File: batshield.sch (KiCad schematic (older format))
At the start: 57 parts, among them J1 mic in, J2 Audio-Jack-2, J3 Audio-Jack-2, J6 Audio-Jack-2, J7 DIN-5_180degree, J8 DIN-5_180degree, SW1 SW_SPDT, SW2 SW_SPDT, SW3 SW_SPDT, SW4 SW_SPST, SW5 SW_Push, SW6 SW_SPST, SW7 SW_Push, SW8 SW_SPST, SW9 SW_Push, U1 LM741, U2 4N35

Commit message: todos los elementos añadidos
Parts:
- removed J?: left up pins, symbol Conn_01x03_Male
- added J?: left up pins, symbol Conn_01x04_Male
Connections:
- net labels added: D7, D8, VIN
- wire segments 154 -> 151
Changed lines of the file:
@@
 	2200 4600 2500 4600
 Wire Wire Line
-	1300 4500 1350 4500
-Wire Wire Line
-	1350 4500 1450 4500
+	1300 4500 1450 4500
 Connection ~ 2900 4100
 Wire Wire Line
@@
 	2900 4850 2900 4800
 Wire Wire Line
-	2750 4800 2900 4800
-Wire Wire Line
-	2900 4800 3000 4800
+	2750 4800 3000 4800
 Wire Wire Line
 	2300 4800 2450 4800
@@
 Connection ~ 4200 4700
 Wire Wire Line
-	4000 4700 4050 4700
-Wire Wire Line
-	4050 4700 4200 4700
-Wire Wire Line
-	4200 4700 4550 4700
+	4000 4700 4550 4700
 Wire Wire Line
 	4200 4350 4200 4150
@@
 	4200 5050 4200 5300
 Wire Wire Line
-	4200 4650 4200 4700
-Wire Wire Line
-	4200 4700 4200 4750
+	4200 4650 4200 4750
 Wire Wire Line
 	3600 4700 3700 4700
@@
 Connection ~ 2900 4600
 Wire Wire Line
-	2900 3950 2900 4100
-Wire Wire Line
-	2900 4100 2900 4600
+	2900 3950 2900 4600
 Wire Wire Line
 	3100 4100 2900 4100
 Wire Wire Line
-	2800 4600 2900 4600
-Wire Wire Line
-	2900 4600 3000 4600
+	2800 4600 3000 4600
 Wire Wire Line
 	1900 1900 4150 1900
@@
 	1900 2100 2100 2100
 Wire Wire Line
-	2400 2100 2550 2100
-Wire Wire Line
-	2550 2100 2950 2100
-Wire Wire Line
-	2950 2100 3100 2100
+	2400 2100 3100 2100
 Connection ~ 3550 3050
 Wire Wire Line
@@
 Connection ~ 4150 2100
 Wire Wire Line
-	3550 3000 3550 3050
-Wire Wire Line
-	3550 3050 3550 3200
-Wire Wire Line
-	2550 3050 3550 3050
-Wire Wire Line
-	3550 3050 4350 3050
+	3550 3000 3550 3200
+Wire Wire Line
+	2550 3050 4350 3050
 Wire Wire Line
 	2550 2500 2550 3050
 Wire Wire Line
-	4000 2100 4150 2100
-Wire Wire Line
-	4150 2100 4450 2100
+	4000 2100 4450 2100
 Wire Wire Line
 	4150 2600 4100 2600
@@
 Connection ~ 3550 2600
 Wire Wire Line
-	3550 2500 3550 2600
-Wire Wire Line
-	3550 2600 3550 2700
-Wire Wire Line
-	3300 2600 3550 2600
-Wire Wire Line
-	3550 2600 3800 2600
+	3550 2500 3550 2700
+Wire Wire Line
+	3300 2600 3800 2600
 Connection ~ 3550 2100
 Wire Wire Line
 	3550 2200 3550 2100
 Wire Wire Line
-	3400 2100 3550 2100
-Wire Wire Line
-	3550 2100 3700 2100
+	3400 2100 3700 2100
 Connection ~ 2550 2100
 Wire Wire Line
@@
 	6050 1250 6300 1250
 Wire Wire Line
-	6600 1250 6750 1250
-Wire Wire Line
-	6750 1250 6950 1250
+	6600 1250 6950 1250
 Wire Wire Line
 	6950 1950 6950 1450
 Wire Wire Line
-	6050 1950 6750 1950
-Wire Wire Line
-	6750 1950 6950 1950
+	6050 1950 6950 1950
 Wire Wire Line
 	6750 1450 6750 1250
@@
 	7750 850  7750 750
 Wire Wire Line
-	7550 1350 7750 1350
-Wire Wire Line
-	7750 1350 7950 1350
+	7550 1350 7950 1350
 Wire Wire Line
 	7750 1150 7750 1350
@@
 	9450 2950 9550 2950
 Wire Wire Line
-	2150 700  2150 900
-Wire Wire Line
-	2150 900  2150 1000
+	2150 700  2150 1000
 Wire Wire Line
 	2150 1350 2150 1300
 Connection ~ 4150 1900
 Wire Wire Line
-	1000 700  1450 700
-Wire Wire Line
-	1450 700  1600 700
+	1000 700  1600 700
 Connection ~ 1450 700
 Wire Wire Line
@@
 	1450 2000 1500 2000
 Wire Wire Line
-	1450 700  1450 900
-Wire Wire Line
-	1450 900  1450 1800
+	1450 700  1450 1800
 Wire Wire Line
 	1450 900  1600 900
 Connection ~ 1450 900
 Wire Wire Line
-	1900 900  2150 900
-Wire Wire Line
-	2150 900  4150 900
+	1900 900  4150 900
 Connection ~ 2150 900
 Wire Wire Line
 	1900 700  2150 700
 Wire Wire Line
-	4150 900  4150 1900
-Wire Wire Line
-	4150 1900 4150 2100
-Wire Wire Line
-	4150 2100 4150 2600
+	4150 900  4150 2600
 Wire Wire Line
 	6200 4500 6100 4500
@@
 	6100 4500 6100 4650
 Wire Wire Line
-	6600 4500 6750 4500
-Wire Wire Line
-	6750 4500 7000 4500
+	6600 4500 7000 4500
 Wire Wire Line
 	6750 4400 6750 4500
@@
 	7400 4500 7400 4650
 Wire Wire Line
-	7900 4500 8050 4500
-Wire Wire Line
-	8050 4500 8300 4500
+	7900 4500 8300 4500
 Wire Wire Line
 	8050 4400 8050 4500
@@
 	8800 4500 8800 4650
 Wire Wire Line
-	9300 4500 9450 4500
-Wire Wire Line
-	9450 4500 9700 4500
+	9300 4500 9700 4500
 Wire Wire Line
 	9450 4400 9450 4500
@@
 	6100 5550 6100 5700
 Wire Wire Line
-	6600 5550 6750 5550
-Wire Wire Line
-	6750 5550 7000 5550
+	6600 5550 7000 5550
 Wire Wire Line
 	6750 5450 6750 5550
@@
 	7400 5550 7400 5700
 Wire Wire Line
-	7900 5550 8050 5550
-Wire Wire Line
-	8050 5550 8300 5550
+	7900 5550 8300 5550
 Wire Wire Line
 	8050 5450 8050 5550
@@
 	8800 5550 8800 5700
 Wire Wire Line
-	9300 5550 9450 5550
-Wire Wire Line
-	9450 5550 9700 5550
+	9300 5550 9700 5550
 Wire Wire Line
 	9450 5450 9450 5550
@@
 F 3 "" H 3850 7000 50  0001 C CNN
 	1    3850 7000
-	1    0    0    -1
-$EndComp
-$Comp
-L Conn_01x03_Male J?
-U 1 1 59DC708D
-P 3850 6350
-F 0 "J?" H 3850 6550 50  0000 C CNN
-F 1 "left up pins" H 3850 6150 50  0000 C CNN
-F 2 "" H 3850 6350 50  0001 C CNN
-F 3 "" H 3850 6350 50  0001 C CNN
-	1    3850 6350
 	1    0    0    -1
 $EndComp
@@
 	1    0    0    -1
 $EndComp
+Text GLabel 4150 7300 2    60   Input ~ 0
+A5
+Text GLabel 4150 7200 2    60   Input ~ 0
+A4
+Text GLabel 4150 7100 2    60   Input ~ 0
+A3
+Text GLabel 4150 7000 2    60   Input ~ 0
+A2
+Text GLabel 4150 6900 2    60   Input ~ 0
+A1
+Text GLabel 4150 6800 2    60   Input ~ 0
+A0
+$Comp
+L Conn_01x04_Male J?
+U 1 1 59DC8B73
+P 3850 6250
+F 0 "J?" H 3850 6450 50  0000 C CNN
+F 1 "left up pins" H 3850 5950 50  0000 C CNN
+F 2 "" H 3850 6250 50  0001 C CNN
+F 3 "" H 3850 6250 50  0001 C CNN
+	1    3850 6250
+	1    0    0    -1
+$EndComp
+Text GLabel 4150 6450 2    60   Input ~ 0
+VIN
+Text GLabel 4150 6350 2    60   Input ~ 0
+GND
+Text GLabel 4150 6250 2    60   Input ~ 0
+GND
+Text GLabel 4150 6150 2    60   Input ~ 0
++5V
+Text GLabel 3250 6300 2    60   Input ~ 0
+GND
+$Comp
+L GND #PWR?
+U 1 1 59DC9304
+P 3150 6350
+F 0 "#PWR?" H 3150 6100 50  0001 C CNN
+F 1 "GND" H 3150 6200 50  0000 C CNN
+F 2 "" H 3150 6350 50  0001 C CNN
+F 3 "" H 3150 6350 50  0001 C CNN
+	1    3150 6350
+	1    0    0    -1
+$EndComp
+Wire Wire Line
+	3250 6300 3150 6300
+Wire Wire Line
+	3150 6300 3150 6350
+Wire Wire Line
+	4050 6150 4150 6150
+Wire Wire Line
+	4050 6250 4150 6250
+Wire Wire Line
+	4050 6350 4150 6350
+Wire Wire Line
+	4050 6450 4150 6450
+Wire Wire Line
+	4050 6800 4150 6800
+Wire Wire Line
+	4050 6900 4150 6900
+Wire Wire Line
+	4050 7000 4150 7000
+Wire Wire Line
+	4050 7100 4150 7100
+Wire Wire Line
+	4050 7200 4150 7200
+Wire Wire Line
+	4050 7300 4150 7300
+Text GLabel 5200 7300 2    60   Input ~ 0
+RX
+Text GLabel 5200 7200 2    60   Input ~ 0
+TX
+Text GLabel 5200 7100 2    60   Input ~ 0
+D2
+Text GLabel 5200 7000 2    60   Input ~ 0
+D3
+Text GLabel 5200 6900 2    60   Input ~ 0
+D4
+Text GLabel 5200 6800 2    60   Input ~ 0
+D5#
+Text GLabel 5200 6700 2    60   Input ~ 0
+D6#
+Text GLabel 5200 6600 2    60   Input ~ 0
+D7
+Text GLabel 5200 6250 2    60   Input ~ 0
+D8
+Text GLabel 5200 6150 2    60   Input ~ 0
+D9
+Text GLabel 5200 6050 2    60   Input ~ 0
+D10
+Text GLabel 5200 5950 2    60   Input ~ 0
+D11
+Text GLabel 5200 5850 2    60   Input ~ 0
+D12
+Text GLabel 5200 5750 2    60   Input ~ 0
+D13
+Text GLabel 5200 5650 2    60   Input ~ 0
+GND
+Wire Wire Line
+	5100 5650 5200 5650
+Wire Wire Line
+	5100 5750 5200 5750
+Wire Wire Line
+	5100 5850 5200 5850
+Wire Wire Line
+	5100 5950 5200 5950
+Wire Wire Line
+	5100 6050 5200 6050
+Wire Wire Line
+	5100 6150 5200 6150
+Wire Wire Line
+	5100 6250 5200 6250
+Wire Wire Line
+	5100 6600 5200 6600
+Wire Wire Line
+	5100 6700 5200 6700
+Wire Wire Line
+	5100 6800 5200 6800
+Wire Wire Line
+	5100 6900 5200 6900
+Wire Wire Line
+	5100 7000 5200 7000
+Wire Wire Line
+	5100 7100 5200 7100
+Wire Wire Line
+	5100 7200 5200 7200
+Wire Wire Line
+	5100 7300 5200 7300
 $EndSCHEMATC

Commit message: power folags
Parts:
- gave numbers to parts that had none: 4
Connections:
- wire segments 151 -> 153
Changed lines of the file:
@@
 $EndComp
 $Comp
-L GND #PWR7
+L GND #PWR8
 U 1 1 59DB61AD
 P 3550 3200
-F 0 "#PWR7" H 3550 2950 50  0001 C CNN
+F 0 "#PWR8" H 3550 2950 50  0001 C CNN
 F 1 "GND" H 3550 3050 50  0000 C CNN
 F 2 "" H 3550 3200 50  0001 C CNN
@@
 +5V
 $Comp
-L GND #PWR8
+L GND #PWR9
 U 1 1 59DB7354
 P 4200 5300
-F 0 "#PWR8" H 4200 5050 50  0001 C CNN
+F 0 "#PWR9" H 4200 5050 50  0001 C CNN
 F 1 "GND" H 4200 5150 50  0000 C CNN
 F 2 "" H 4200 5300 50  0001 C CNN
@@
 RX
 $Comp
-L GND #PWR15
+L GND #PWR16
 U 1 1 59DBACB5
 P 7750 1800
-F 0 "#PWR15" H 7750 1550 50  0001 C CNN
+F 0 "#PWR16" H 7750 1550 50  0001 C CNN
 F 1 "GND" H 7750 1650 50  0000 C CNN
 F 2 "" H 7750 1800 50  0001 C CNN
@@
 MIDI out\n(http://www.instructables.com/id/\nSend-and-Receive-MIDI-with-Arduino/)
 $Comp
-L GND #PWR21
+L GND #PWR22
 U 1 1 59DBC11B
 P 10000 1550
-F 0 "#PWR21" H 10000 1300 50  0001 C CNN
+F 0 "#PWR22" H 10000 1300 50  0001 C CNN
 F 1 "GND" H 10000 1400 50  0000 C CNN
 F 2 "" H 10000 1550 50  0001 C CNN
@@
 $EndComp
 $Comp
-L GND #PWR11
+L GND #PWR12
 U 1 1 59DBCB38
 P 6400 3150
-F 0 "#PWR11" H 6400 2900 50  0001 C CNN
+F 0 "#PWR12" H 6400 2900 50  0001 C CNN
 F 1 "GND" H 6400 3000 50  0000 C CNN
 F 2 "" H 6400 3150 50  0001 C CNN
@@
 $EndComp
 $Comp
-L GND #PWR12
+L GND #PWR13
 U 1 1 59DBD259
 P 7150 3150
-F 0 "#PWR12" H 7150 2900 50  0001 C CNN
+F 0 "#PWR13" H 7150 2900 50  0001 C CNN
 F 1 "GND" H 7150 3000 50  0000 C CNN
 F 2 "" H 7150 3150 50  0001 C CNN
@@
 $EndComp
 $Comp
-L GND #PWR16
+L GND #PWR17
 U 1 1 59DBD2BB
 P 7900 3150
-F 0 "#PWR16" H 7900 2900 50  0001 C CNN
+F 0 "#PWR17" H 7900 2900 50  0001 C CNN
 F 1 "GND" H 7900 3000 50  0000 C CNN
 F 2 "" H 7900 3150 50  0001 C CNN
@@
 $EndComp
 $Comp
-L GND #PWR17
+L GND #PWR18
 U 1 1 59DBD332
 P 8600 3150
-F 0 "#PWR17" H 8600 2900 50  0001 C CNN
+F 0 "#PWR18" H 8600 2900 50  0001 C CNN
 F 1 "GND" H 8600 3000 50  0000 C CNN
 F 2 "" H 8600 3150 50  0001 C CNN
@@
 $EndComp
 $Comp
-L GND #PWR20
+L GND #PWR21
 U 1 1 59DBD3BA
 P 9300 3150
-F 0 "#PWR20" H 9300 2900 50  0001 C CNN
+F 0 "#PWR21" H 9300 2900 50  0001 C CNN
 F 1 "GND" H 9300 3000 50  0000 C CNN
 F 2 "" H 9300 3150 50  0001 C CNN
@@
 $EndComp
 $Comp
-L GND #PWR9
+L GND #PWR10
 U 1 1 59DC0BCD
 P 6100 4650
-F 0 "#PWR9" H 6100 4400 50  0001 C CNN
+F 0 "#PWR10" H 6100 4400 50  0001 C CNN
 F 1 "GND" H 6100 4500 50  0000 C CNN
 F 2 "" H 6100 4650 50  0001 C CNN
@@
 $EndComp
 $Comp
-L GND #PWR13
+L GND #PWR14
 U 1 1 59DC1485
 P 7400 4650
-F 0 "#PWR13" H 7400 4400 50  0001 C CNN
+F 0 "#PWR14" H 7400 4400 50  0001 C CNN
 F 1 "GND" H 7400 4500 50  0000 C CNN
 F 2 "" H 7400 4650 50  0001 C CNN
@@
 $EndComp
 $Comp
-L GND #PWR18
+L GND #PWR19
 U 1 1 59DC1541
 P 8800 4650
-F 0 "#PWR18" H 8800 4400 50  0001 C CNN
+F 0 "#PWR19" H 8800 4400 50  0001 C CNN
 F 1 "GND" H 8800 4500 50  0000 C CNN
 F 2 "" H 8800 4650 50  0001 C CNN
@@
 $EndComp
 $Comp
-L GND #PWR10
+L GND #PWR11
 U 1 1 59DC1607
 P 6100 5700
-F 0 "#PWR10" H 6100 5450 50  0001 C CNN
+F 0 "#PWR11" H 6100 5450 50  0001 C CNN
 F 1 "GND" H 6100 5550 50  0000 C CNN
 F 2 "" H 6100 5700 50  0001 C CNN
@@
 $EndComp
 $Comp
-L GND #PWR14
+L GND #PWR15
 U 1 1 59DC1828
 P 7400 5700
-F 0 "#PWR14" H 7400 5450 50  0001 C CNN
+F 0 "#PWR15" H 7400 5450 50  0001 C CNN
 F 1 "GND" H 7400 5550 50  0000 C CNN
 F 2 "" H 7400 5700 50  0001 C CNN
@@
 $EndComp
 $Comp
-L GND #PWR19
+L GND #PWR20
 U 1 1 59DC18FA
 P 8800 5700
-F 0 "#PWR19" H 8800 5450 50  0001 C CNN
+F 0 "#PWR20" H 8800 5450 50  0001 C CNN
 F 1 "GND" H 8800 5550 50  0000 C CNN
 F 2 "" H 8800 5700 50  0001 C CNN
@@
 Text Notes 900  5850 0    60   ~ 0
 Digital / PWM output
-Text Notes 3400 5750 0    60   ~ 0
+Text Notes 3850 5750 0    60   ~ 0
 Arduino pins
 Connection ~ 4050 4700
@@
 	1150 6050 1450 6050
 $Comp
-L Conn_01x06_Male J?
+L Conn_01x06_Male J5
 U 1 1 59DC6FFA
 P 3850 7000
-F 0 "J?" H 3850 7300 50  0000 C CNN
+F 0 "J5" H 3850 7300 50  0000 C CNN
 F 1 "left down pins" H 3850 6600 50  0000 C CNN
 F 2 "" H 3850 7000 50  0001 C CNN
@@
 $EndComp
 $Comp
-L Conn_01x08_Male J?
+L Conn_01x08_Male J10
 U 1 1 59DC720C
 P 4900 6900
-F 0 "J?" H 4900 7300 50  0000 C CNN
+F 0 "J10" H 4900 7300 50  0000 C CNN
 F 1 "rigth donw pins" H 4900 6400 50  0000 C CNN
 F 2 "" H 4900 6900 50  0001 C CNN
@@
 $EndComp
 $Comp
-L Conn_01x07_Male J?
+L Conn_01x07_Male J9
 U 1 1 59DC7310
 P 4900 5950
-F 0 "J?" H 4900 6350 50  0000 C CNN
+F 0 "J9" H 4900 6350 50  0000 C CNN
 F 1 "rigth up pins" H 4900 5550 50  0000 C CNN
 F 2 "" H 4900 5950 50  0001 C CNN
@@
 A0
 $Comp
-L Conn_01x04_Male J?
+L Conn_01x04_Male J4
 U 1 1 59DC8B73
 P 3850 6250
-F 0 "J?" H 3850 6450 50  0000 C CNN
+F 0 "J4" H 3850 6450 50  0000 C CNN
 F 1 "left up pins" H 3850 5950 50  0000 C CNN
 F 2 "" H 3850 6250 50  0001 C CNN
@@
 Text GLabel 4150 6150 2    60   Input ~ 0
 +5V
-Text GLabel 3250 6300 2    60   Input ~ 0
+Text GLabel 3050 6300 2    60   Input ~ 0
 GND
 $Comp
-L GND #PWR?
+L GND #PWR7
 U 1 1 59DC9304
-P 3150 6350
-F 0 "#PWR?" H 3150 6100 50  0001 C CNN
-F 1 "GND" H 3150 6200 50  0000 C CNN
-F 2 "" H 3150 6350 50  0001 C CNN
-F 3 "" H 3150 6350 50  0001 C CNN
-	1    3150 6350
-	1    0    0    -1
-$EndComp
-Wire Wire Line
-	3250 6300 3150 6300
-Wire Wire Line
-	3150 6300 3150 6350
+P 2950 6350
+F 0 "#PWR7" H 2950 6100 50  0001 C CNN
+F 1 "GND" H 2950 6200 50  0000 C CNN
+F 2 "" H 2950 6350 50  0001 C CNN
+F 3 "" H 2950 6350 50  0001 C CNN
+	1    2950 6350
+	1    0    0    -1
+$EndComp
+Wire Wire Line
+	3050 6300 2950 6300
+Wire Wire Line
+	2950 6300 2950 6350
 Wire Wire Line
 	4050 6150 4150 6150
@@
 Wire Wire Line
 	5100 7300 5200 7300
+$Comp
+L PWR_FLAG #FLG?
+U 1 1 59DCD561
+P 2800 6950
+F 0 "#FLG?" H 2800 7025 50  0001 C CNN
+F 1 "PWR_FLAG" H 2800 7100 50  0000 C CNN
+F 2 "" H 2800 6950 50  0001 C CNN
+F 3 "" H 2800 6950 50  0001 C CNN
+	1    2800 6950
+	1    0    0    -1
+$EndComp
+Text GLabel 2800 7050 3    60   Input ~ 0
+GND
+Wire Wire Line
+	2800 7050 2800 6950
+Text GLabel 3250 7050 3    60   Input ~ 0
++5V
+$Comp
+L PWR_FLAG #FLG?
+U 1 1 59DCD8D5
+P 3250 6950
+F 0 "#FLG?" H 3250 7025 50  0001 C CNN
+F 1 "PWR_FLAG" H 3250 7100 50  0000 C CNN
+F 2 "" H 3250 6950 50  0001 C CNN
+F 3 "" H 3250 6950 50  0001 C CNN
+	1    3250 6950
+	1    0    0    -1
+$EndComp
+Wire Wire Line
+	3250 7050 3250 6950
 $EndSCHEMATC

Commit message: corrección salida audio
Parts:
- removed J4: left up pins, symbol Conn_01x04_Male
- removed J9: rigth up pins, symbol Conn_01x07_Male
- added J11: service power, symbol Conn_01x04_Male
- added J4: left uppins, symbol Conn_01x06_Male
- added J9: rigth up pins, symbol Conn_01x08_Male
- added R23, R24: 10k, symbol R
- added SW10, SW11: SW_SPST, symbol SW_SPST
- added SW12: SW_Push, symbol SW_Push
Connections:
- net labels added: +3V3, RESET
- wire segments 153 -> 173
- no-connect marks 8 -> 9
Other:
- moved on the sheet: R14, R15, R17, R18, R19, R20, SW4, SW5, SW6, SW7, SW8, SW9

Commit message: preamp para guitarra
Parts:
- removed R1: 10k, symbol R
- added C? (x4): C, symbol C
- added C?: CP, symbol CP
- added J?: mic in, symbol Audio-Jack-2
- added R? (x6): R, symbol R
- added RV?: POT, symbol POT
- added U?: TL072, symbol TL072
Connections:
- net +5V: now also U?.8 (V+)
- net A0: now also C?.1, R?.1
- net D2: no longer R14.2, SW4.2 (B)
- net GND: now also SW10.2 (B), C?.2, C?.2, C?.2, J?.2, R?.2, U?.4 (V-); no longer SW10.1 (A)
- net RESET: now also SW10.1 (A); no longer SW10.2 (B)
- net D10 renamed D10#
- net D9 renamed D9#
- new net: R14.2, SW4.2 (B)
- new net: C?.2, J?.1, R?.1
- new net: C?.1, R?.1, R?.2, U?.1
- new net: C?.2, R?.2, RV?.2, RV?.3, U?.2 (-)
- new net: C?.1, R?.1, U?.3 (+)
- new net: C?.1, R?.1, R?.2
- new net: C?.1, R?.1
- new net: R?.2, RV?.1
- new net 2.5V: R?.2
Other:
- note added: "guitar preamp\n(https://create.arduino.cc/projecthub/electrosmash/arduino-uno-guitar-pedal-b2ba96)"
- moved on the sheet: D1, J10, J11, J2, J3, J4, J5, J7, J8, J9, R13, R14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

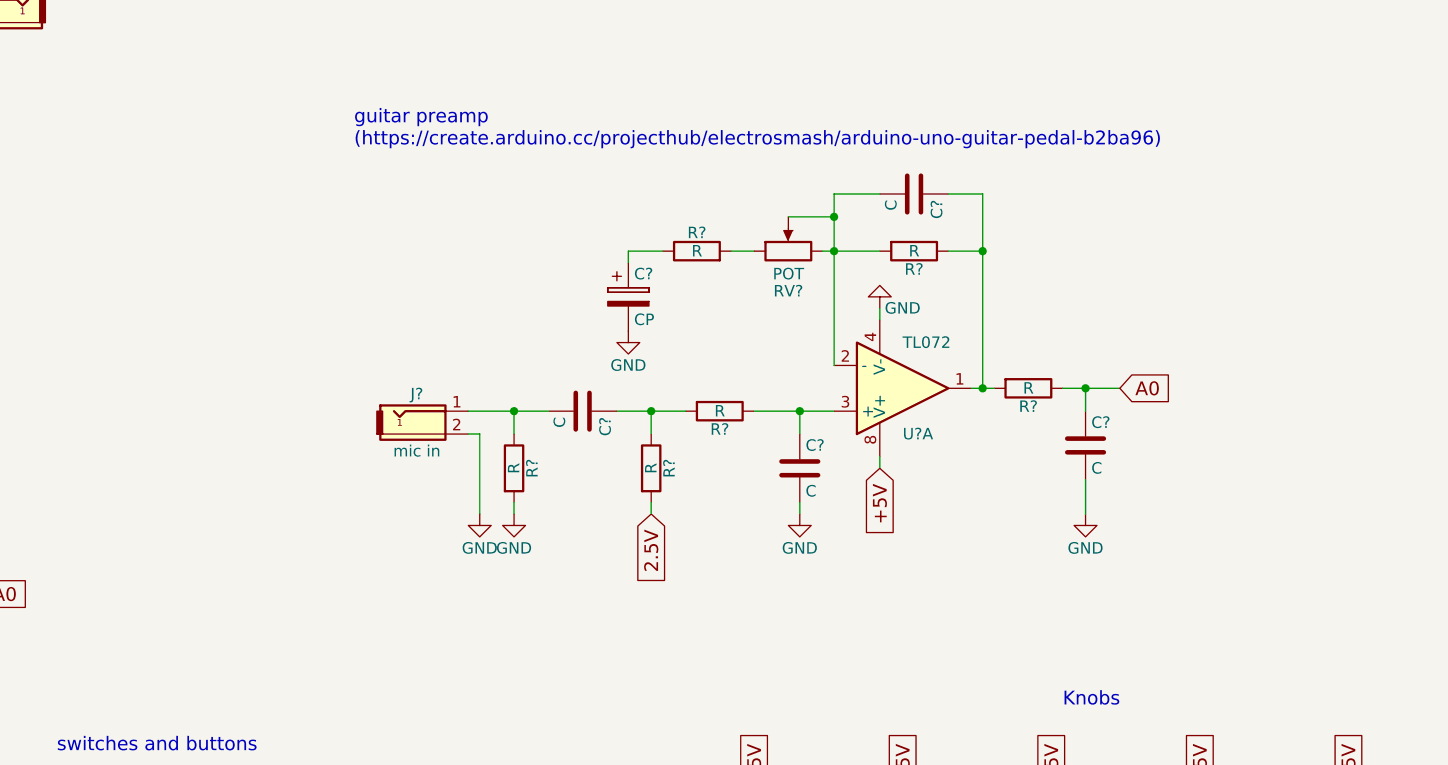
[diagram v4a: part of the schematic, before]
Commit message: simulaciones spice y preamplificador per tutto
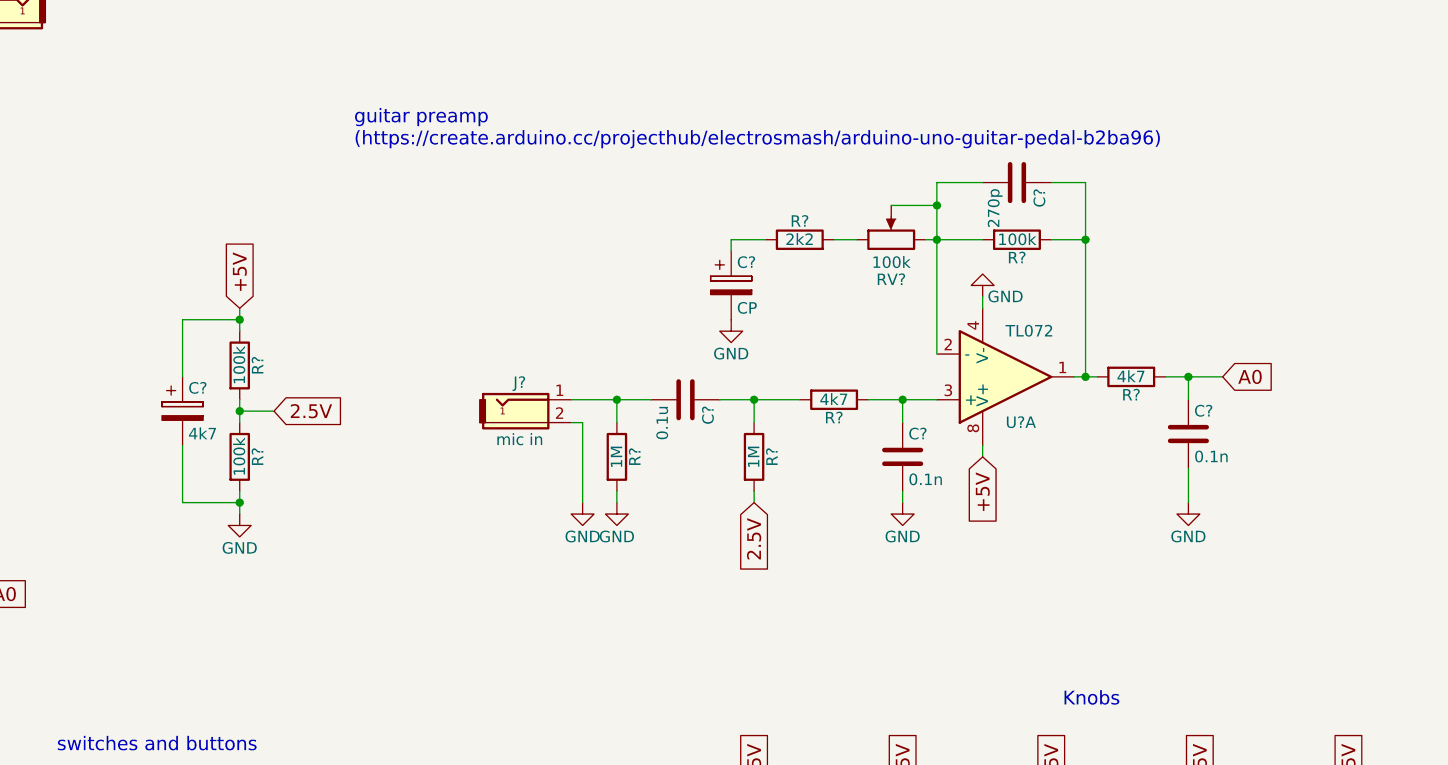
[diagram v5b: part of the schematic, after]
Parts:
- added C?: 4k7, symbol CP
- added R? (x2): 100k, symbol R
- C?: value C -> 0.1u
- C? (x2): value C -> 0.1n
- C?: value C -> 270p
- R? (x2): value R -> 1M
- R?: value R -> 2k2
- R? (x2): value R -> 4k7
- R?: value R -> 100k
- RV?: value POT -> 100k
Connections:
- net +5V: now also C?.1, R?.1
- net 2.5V: now also R?.1, R?.2
- net GND: now also C?.2, R?.2
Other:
- moved on the sheet: C?, J?, R?, RV?, U?A
